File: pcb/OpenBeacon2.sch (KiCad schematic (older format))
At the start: 78 parts, among them J1 Bias V, J10 UART, J11 BNC, J2 PAI+, J3 PAI-, J4 Digital IO, J5 ADC Inputs, J6 SMA, J8 I2C Bus, J9 GND, K1 G5V-1-DC5, K2 G5V-1-DC5, M1 LPF 1, M2 LPF 2, Q1 2N7002, Q2 MMBT4403, Q3 2SK3074, Q4 2N7002, Q5 2N7002, Q6 2N7002, U1 TLV61046A, U2 ASTX-H11-25.000MHZ-T, U3 SN74LVC1G17, U4 SI5351A, U5 MCP4725A1T-E/CH, U6 128x32 OLED, U7 Empyrean, U8 24AA64T

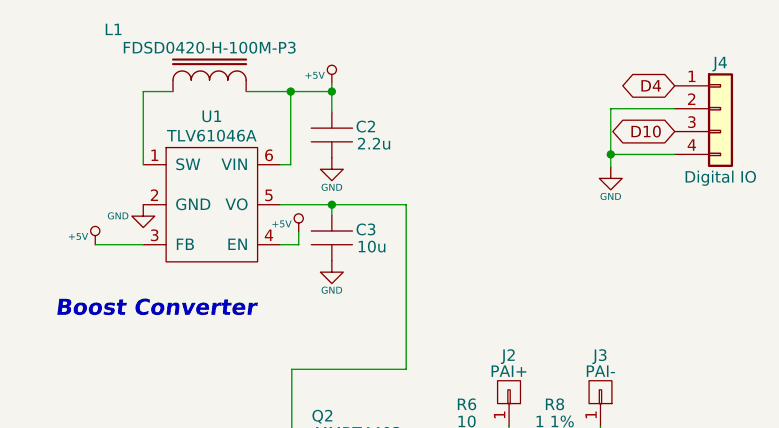
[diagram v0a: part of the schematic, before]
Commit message: Fix fw where freq would show as 0 during startup
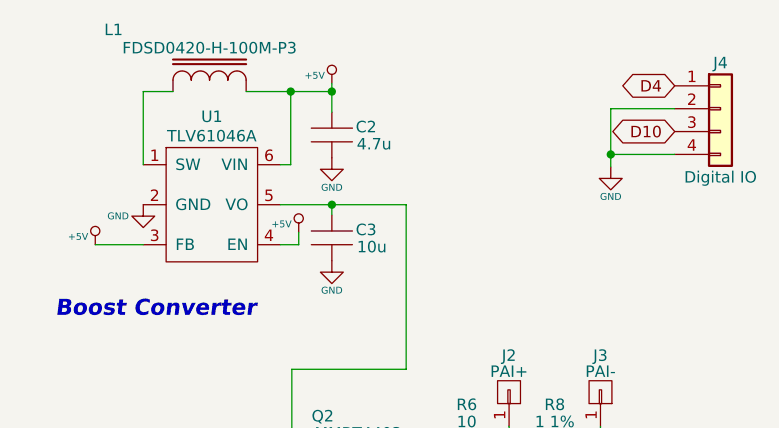
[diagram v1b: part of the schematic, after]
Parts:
- C2: value 2.2u -> 4.7u
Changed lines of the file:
@@
 Sheet 1 1
 Title "OpenBeacon 2"
-Date "2019-09-17"
+Date "2019-09-18"
 Rev "B"
 Comp "Etherkit"
@@
 P 2175 1110
 F 0 "C2" H 2325 1145 50  0000 C CNN
-F 1 "2.2u" H 2360 1070 50  0000 C CNN
+F 1 "4.7u" H 2360 1070 50  0000 C CNN
 F 2 "Capacitor_SMD:C_0805_2012Metric" H 2175 1110 60  0001 C CNN
 F 3 "" H 2175 1110 60  0000 C CNN
